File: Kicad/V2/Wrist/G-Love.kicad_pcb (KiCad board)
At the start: 2 copper layers, 36 x 36 mm, 154 parts, among them J5 XLR5_Ground, U1 ATMega328P, U10 6N137, U11 MAX485E, U12 TPS2113APWR, U13 AMS1117, U2 ICM-42688-P_I2C, U3 TXS0104E, U4 Hall Sensor A3144, U5 ATMEGA2561-16AU, U6 TUSB321, U7 74HC4052, U8 74HC4052, U9 B0505S-1W1, Y1 16MHz, Y2 16MHz

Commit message: j'aurai du commit avant, j'ai tunnel
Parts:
- removed C24, C25, C26, C33, C34, C35, C36, C37, C39, C40, C42, C43, C47, C49, C51: 100nF, MyGlove:Capacitor_0603
- removed C27, C28: 47pF, MyGlove:Capacitor_0603
- removed C29, C30, C38, C41, C48: 4.7uF, MyGlove:Capacitor_Electrolytic
- removed C31: 10nF, MyGlove:Capacitor_0603
- removed C32: 10n, MyGlove:Capacitor_0603
- removed C44, C45, C46: 1uF, MyGlove:Capacitor_0603
- removed C50: 10uF, MyGlove:Capacitor_0603
- removed D2, D5, D6: YELLOW, MyGlove:LED
- removed D3, D4: RED, MyGlove:LED
- removed FSR_1, FSR_2, FSR_3, FSR_4, FSR_5, FS_1, FS_2, FS_3, FS_4, FS_5, FS_6: ~, MyGlove:PinHeader_1x02_P2.54mm_Vertical
- removed J4: ~, MyGlove:PinHeader_1x06_P2.54mm_Vertical
- removed J5: XLR5_Ground, MyGlove:XLR5_Connector_Female_CONN-TH_NC5FAH
- removed J_1, J_2: Conn_USB_Receptacle, MyGlove:USB_C_Receptacle_GCT_USB4105-xx-A_16P_TopMnt_Horizontal
- removed J_3: ~, MyGlove:PinHeader_1x04_P2.54mm_Vertical
- removed R19, R28, R37, R39: 10kΩ, MyGlove:Resistor_0603
- removed R20, R21, R30, R31, R32, R33: 1k, MyGlove:Resistor_0603
- removed R22, R23: 1M, MyGlove:Resistor_0603
- removed R24, R25, R26, R27: 5.1k, MyGlove:Resistor_0603
- removed R29: 900K, MyGlove:Resistor_0805
- removed R34: 330R, MyGlove:Resistor_0603
- removed R35: 4.7k, MyGlove:Resistor_0603
- removed R36: 560R, MyGlove:Resistor_0603
- removed R38: 47k, MyGlove:Resistor_0603
- removed the REF** at (212.2, 90.5)
- removed the REF** at (187.8, 90.5)
- removed the REF** at (187.8, 109.5)
- removed the REF** at (212.2, 109.5)
- removed SW_1, SW_2: ~, MyGlove:SW_SPST_TL3305A
- removed TP1, TP10, TP11, TP12, TP13, TP14, TP15, TP16, TP17, TP18, TP2, TP3, TP4, TP5, TP6, TP7, TP8, TP9: ~, MyGlove:TestPoint_Pad_D1.0mm
- removed U10: 6N137, MyGlove:6N137
- removed U11: MAX485E, MyGlove:MAX485ED
- removed U12: TPS2113APWR, MyGlove:TPS2113
- removed U13: AMS1117, MyGlove:AMS1117
- removed U3: TXS0104E, MyGlove:TXS0104EPWR
- removed U4: Hall Sensor A3144, MyGlove:PinHeader_1x03_P2.54mm_Vertical
- removed U5: ATMEGA2561-16AU, MyGlove:ATMega2561
- removed U6: TUSB321, Package_DFN_QFN:Texas_X2QFN-12_1.6x1.6mm_P0.4mm
- removed U7, U8: 74HC4052, MyGlove:74HC4052
- removed U9: B0505S-1W1, MyGlove:B0505S
- removed U_1: CH340K, MyGlove:CH340K
- removed Y2: 16MHz, MyGlove:Crystal_16MHz
- added J01: ~, MyGlove:FPC 14, F.Cu at (133.5, 91.5)
- added J04: SM12B-SRSS-TB(LF)(SN), MyGlove:JST 12 Pin, F.Cu at (187.0, 100.0)
- added J2: ~, MyGlove:PinHeader_1x06_P2.54mm_Vertical, F.Cu at (193.6, 116.5)
- added J6: ~, MyGlove:JST 4 Pin, F.Cu at (200.1, 85.9)
- added REF**: Watch mount hole, G-Love:Watch mount hole, F.Cu at (200.0, 100.0)
- added U03: TXS0102DCUR, MyGlove:LVL SHIFTER TXS0102DCUR, F.Cu at (208.2, 93.2)
- C10: value 0.1nF -> 12pF
- C11, C12: value 47pF -> 100nF
- C13, C14, C15, C16, C17, C18, C19: value 47pF -> 10nF
- C2: value 100nF -> 10uF
- C20, C21: value 12pF -> 10nF
- C22: value 100nF -> 10nF
- C6, C7: value 12pF -> 100nF
- C8: value 10nF -> 100nF
- C9: value 2.2nF -> 12pF
- CD1: footprint MyGlove:CD4097B -> MyGlove:CD4097BPW
- D1: value YELLOW -> ~; footprint MyGlove:LED -> MyGlove:TVS_DIODE
- J3: footprint MyGlove:PinHeader_1x11_P2.54mm_Vertical -> MyGlove:FPC_CONNECTOR_24
- R1, R2: value 2.2kΩ -> 2.2K
- R3: value 1K -> 10kΩ
- R4: value 1K -> 330R
- R5: value 10kΩ -> 330R
- R8: value 10kΩ -> 10K
- U1: value ATMega328P -> XC6206P332MR-G; footprint MyGlove:ATMega328P-AU -> MyGlove:LDO Mini
- U2: value ICM-42688-P_I2C -> ATMega328P; footprint MyGlove:ICM-42688-P -> MyGlove:ATMega328P-AU
- moved C11 111.6 mm to (207.4, 89.1), turned to 90 degrees
- moved R8 108.1 mm to (205.9, 94.3), turned to 90 degrees
- moved C20 97.1 mm to (206.7, 107.0), turned to 180 degrees
- moved C21 97.0 mm to (206.7, 108.5), turned to 180 degrees
- moved C22 97.0 mm to (206.7, 110.0), turned to 180 degrees
- moved R17 89.7 mm to (209.8, 108.5), turned to 180 degrees
- moved J3 87.0 mm to (212.7, 100.0), turned to -90 degrees
- moved C23 87.0 mm to (196.5, 113.9)
- moved R16 83.6 mm to (209.8, 107.0), turned to 180 degrees
- moved C19 78.5 mm to (206.7, 105.5), turned to 180 degrees
- moved R12 71.3 mm to (209.8, 101.0), turned to 180 degrees
- moved C15 66.3 mm to (206.7, 99.5), turned to 180 degrees
- moved C4 66.0 mm to (203.0, 98.9), turned to 180 degrees
- moved R5 61.3 mm to (200.7, 91.9)
- moved R18 60.7 mm to (209.8, 110.0), turned to 180 degrees
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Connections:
- C1 pad 1: GND -> VCC
- C1 pad 2: Net-(U1-AREF) -> GND
- C10 pad 1: +3.3V -> GND
- C10 pad 2: GND -> Net-(U2-XTAL2/TOSC2/PCINT7/PB7)
- C11 pad 1: GND -> +3.3V
- C11 pad 2: /Hand_Captors/Flex_Sensor4/FlexADC -> GND
- C12 pad 1: GND -> VCC
- C12 pad 2: /Hand_Captors/Flex_Sensor3/FlexADC -> GND
- C13 pad 1: GND -> /Hand_Captors/hand_captors/FORCE_THUMB_IN
- C13 pad 2: /Hand_Captors/Flex_Sensor2/FlexADC -> GND
- C14 pad 1: GND -> /Hand_Captors/hand_captors/FLEX_THUMB_IN
- C14 pad 2: /Hand_Captors/Flex_Sensor0/FlexADC -> GND
- C15 pad 1: GND -> /Hand_Captors/hand_captors/FORCE_INDEX_IN
- C15 pad 2: /Hand_Captors/FSR_Index/TouchADC -> GND
- C16 pad 1: GND -> /Hand_Captors/hand_captors/FLEX_INDEX_IN
- C16 pad 2: /Hand_Captors/FSR_Little/TouchADC -> GND
- C17 pad 1: GND -> /Hand_Captors/hand_captors/FORCE_MIDDLE_IN
- C17 pad 2: /Hand_Captors/FSR_Ring/TouchADC -> GND
- C18 pad 1: GND -> /Hand_Captors/hand_captors/FLEX_MIDDLE_IN
- C18 pad 2: /Hand_Captors/FSR_Thumb/TouchADC -> GND
- C19 pad 1: GND -> /Hand_Captors/hand_captors/FORCE_RING_IN
- C19 pad 2: /Hand_Captors/Flex_Sensor5/FlexADC -> GND
- C2 pad 2: VCC -> +3.3V
- C20 pad 1: Net-(U5-XTAL2) -> /Hand_Captors/hand_captors/FLEX_RING_IN
- C21 pad 1: GND -> /Hand_Captors/hand_captors/FORCE_LITTLE_IN
- C21 pad 2: Net-(U5-XTAL1) -> GND
- C22 pad 1: GND -> /Hand_Captors/hand_captors/FLEX_LITTLE_IN
- C22 pad 2: Net-(C22-Pad2) -> GND
- C23 pad 1: /ATMega2561/MCU_2561_RESET -> VCC
- C23 pad 2: /ATMega2561/DTR -> GND
- C3 pad 2: VCC -> +3.3V
- C4 pad 2: Net-(C4-Pad2) -> Net-(U2-AREF)
- C5 pad 1: VCC -> GND
- C5 pad 2: GND -> VCC
- C6 pad 2: Net-(U1-XTAL1/TOSC1/PCINT6/PB6) -> VCC
- C7 pad 2: Net-(U1-XTAL2/TOSC2/PCINT7/PB7) -> /ATmega328p/MCU_328P_RESET
- C8 pad 1: GND -> VCC
- C8 pad 2: +3.3V -> GND
- C9 pad 1: +3.3V -> GND
- C9 pad 2: GND -> Net-(U2-XTAL1/TOSC1/PCINT6/PB6)
- CD1 pad 18: /Hand_Captors/Flex_Sensor5/FlexADC -> /Hand_Captors/hand_captors/HALL_IN
- CD1 pad 19: /Hand_Captors/Flex_Sensor4/FlexADC -> /Hand_Captors/hand_captors/FORCE_LITTLE_IN
- CD1 pad 20: /Hand_Captors/Flex_Sensor3/FlexADC -> /Hand_Captors/hand_captors/FORCE_RING_IN
- CD1 pad 21: /Hand_Captors/Flex_Sensor2/FlexADC -> /Hand_Captors/hand_captors/FORCE_MIDDLE_IN
- CD1 pad 22: /Hand_Captors/Flex_Sensor1/FlexADC -> /Hand_Captors/hand_captors/FORCE_INDEX_IN
- CD1 pad 23: /Hand_Captors/Flex_Sensor0/FlexADC -> /Hand_Captors/hand_captors/FORCE_THUMB_IN
- CD1 pad 4: /Hand_Captors/HallCaptor/HallGPIO_Clasp -> unconnected-(CD1-X_5-Pad4)
- CD1 pad 5: /Hand_Captors/FSR_Little/TouchADC -> /Hand_Captors/hand_captors/FLEX_LITTLE_IN
- CD1 pad 6: /Hand_Captors/FSR_Ring/TouchADC -> /Hand_Captors/hand_captors/FLEX_RING_IN
- CD1 pad 7: /Hand_Captors/FSR_Middle/TouchADC -> /Hand_Captors/hand_captors/FLEX_MIDDLE_IN
- CD1 pad 8: /Hand_Captors/FSR_Index/TouchADC -> /Hand_Captors/hand_captors/FLEX_INDEX_IN
- CD1 pad 9: /Hand_Captors/FSR_Thumb/TouchADC -> /Hand_Captors/hand_captors/FLEX_THUMB_IN
- D1 pad 1: Net-(D1-A) -> /ATmega328p/MISO_BOOT_328P
- D1 pad 2: /ATMega2561/2561_TXD1 -> /ATmega328p/SCK_BOOT_328P
- J3 pad 1: GND -> VCCL
- J3 pad 10: /ATMega2561/2561_MOSI -> Net-(U03-A2)
- J3 pad 11: VCC -> GND
- J3 pad 2: /ATMega2561/2561_TOUCH_INT -> VCCL
- J3 pad 3: /ATMega2561/2561_TOUCH_RESET -> GND
- J3 pad 4: /ATMega2561/2561_SDA -> GND
- J3 pad 5: /ATMega2561/2561_SCL -> /ATmega328p/MISO_BOOT_328P
- J3 pad 6: /ATMega2561/2561_SS -> /ATmega328p/SCK_BOOT_328P
- J3 pad 7: /ATMega2561/2561_SCREEN_DC -> GND
- J3 pad 8: /ATMega2561/2561_SCREEN_RESET -> +3.3V
- J3 pad 9: /ATMega2561/SCK_BOOT_2561 -> Net-(U03-A1)
- R1 pad 1: /ATMega2561/2561_SCL -> /ATmega328p/328P_I2C_IMU_SDA
- R10 pad 1: /Hand_Captors/Flex_Sensor2/FlexADC -> /Hand_Captors/hand_captors/FLEX_THUMB_IN
- R11 pad 1: /Hand_Captors/Flex_Sensor0/FlexADC -> /Hand_Captors/hand_captors/FORCE_INDEX_IN
- R12 pad 1: GND -> /Hand_Captors/hand_captors/FLEX_INDEX_IN
- R12 pad 2: /Hand_Captors/FSR_Index/TouchADC -> GND
- R13 pad 1: GND -> /Hand_Captors/hand_captors/FORCE_MIDDLE_IN
- R13 pad 2: /Hand_Captors/FSR_Little/TouchADC -> GND
- R14 pad 1: GND -> /Hand_Captors/hand_captors/FLEX_MIDDLE_IN
- R14 pad 2: /Hand_Captors/FSR_Ring/TouchADC -> GND
- R15 pad 1: GND -> /Hand_Captors/hand_captors/FORCE_RING_IN
- R15 pad 2: /Hand_Captors/FSR_Thumb/TouchADC -> GND
- R16 pad 1: /Hand_Captors/Flex_Sensor5/FlexADC -> /Hand_Captors/hand_captors/FLEX_RING_IN
- R17 pad 1: /ATMega2561/MCU_2561_RESET -> /Hand_Captors/hand_captors/FORCE_LITTLE_IN
- R17 pad 2: VCC -> GND
- R18 pad 1: /Hand_Captors/Flex_Sensor1/FlexADC -> /Hand_Captors/hand_captors/FLEX_LITTLE_IN
- R2 pad 1: /ATMega2561/2561_SDA -> /ATmega328p/328P_I2C_IMU_SCL
- R3 pad 1: Net-(D1-A) -> /ATmega328p/MCU_328P_RESET
- R4 pad 1: Net-(D2-A) -> Net-(U2-OC2A/MOSI/PCINT3/PB3)
- R4 pad 2: VCC -> /ATmega328p/MISO_BOOT_328P
- R5 pad 1: /ATmega328p/MCU_328P_RESET -> Net-(U2-SCK/PCINT5/PB5)
- R5 pad 2: VCC -> /ATmega328p/SCK_BOOT_328P
- R8 pad 1: /Hand_Captors/Flex_Sensor4/FlexADC -> /Hand_Captors/hand_captors/HALL_IN
- R8 pad 2: GND -> VCC
- R9 pad 1: /Hand_Captors/Flex_Sensor3/FlexADC -> /Hand_Captors/hand_captors/FORCE_THUMB_IN
- U1 pad 1: unconnected-(U1-OC2B/INT1/PCINT19/PD3-Pad1) -> GND
- U1 pad 2: unconnected-(U1-XCK/T0/PCINT20/PD4-Pad2) -> +3.3V
- U1 pad 3: GND -> VCC
- U2 pad 11: GND -> unconnected-(U2-AIN1/PCINT23/PD7-Pad11)
- U2 pad 12: +3.3V -> unconnected-(U2-ICP1/CLK0/PCINT0/PB0-Pad12)
- U2 pad 13: Net-(U2-AP_SCK) -> unconnected-(U2-OC1A/PCINT1/PB1-Pad13)
- U2 pad 14: Net-(U2-AP_SDA) -> unconnected-(U2-OC1B/~{SS}/PCINT2/PB2-Pad14)
- U2 pad 3: unconnected-(U2-RESV-Pad3) -> GND
- U2 pad 4: unconnected-(U2-INT1/INT-Pad4) -> VCC
- U2 pad 5: +3.3V -> GND
- U2 pad 6: GND -> VCC
- U2 pad 7: GND -> Net-(U2-XTAL1/TOSC1/PCINT6/PB6)
- U2 pad 8: +3.3V -> Net-(U2-XTAL2/TOSC2/PCINT7/PB7)
- Y1 pad 1: Net-(U1-XTAL1/TOSC1/PCINT6/PB6) -> Net-(U2-XTAL1/TOSC1/PCINT6/PB6)
- Y1 pad 3: Net-(U1-XTAL2/TOSC2/PCINT7/PB7) -> Net-(U2-XTAL2/TOSC2/PCINT7/PB7)
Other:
- board size 36 x 36 mm -> 39 x 39 mm
- board text added: "Ajouter Testpoints / 0Ohm pour reverse, 0603 en série"

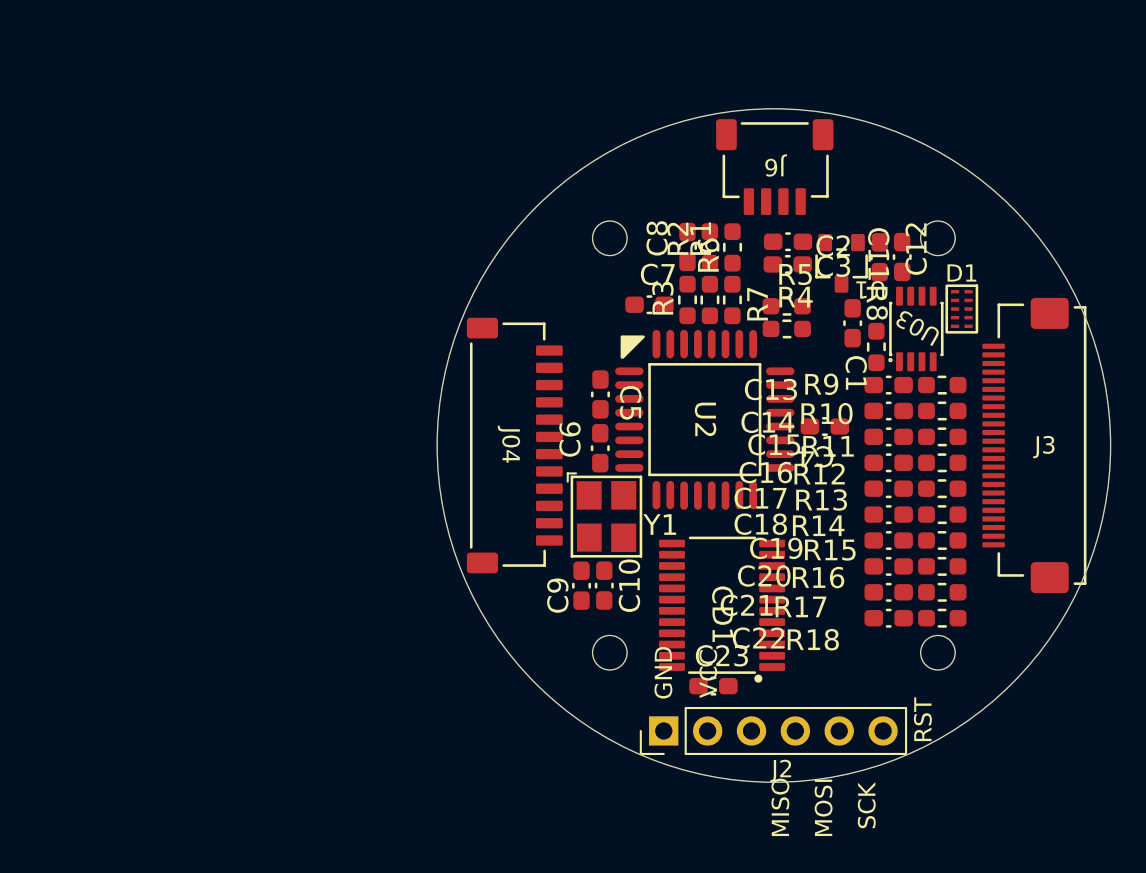
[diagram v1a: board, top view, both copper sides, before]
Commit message: Routing ADC
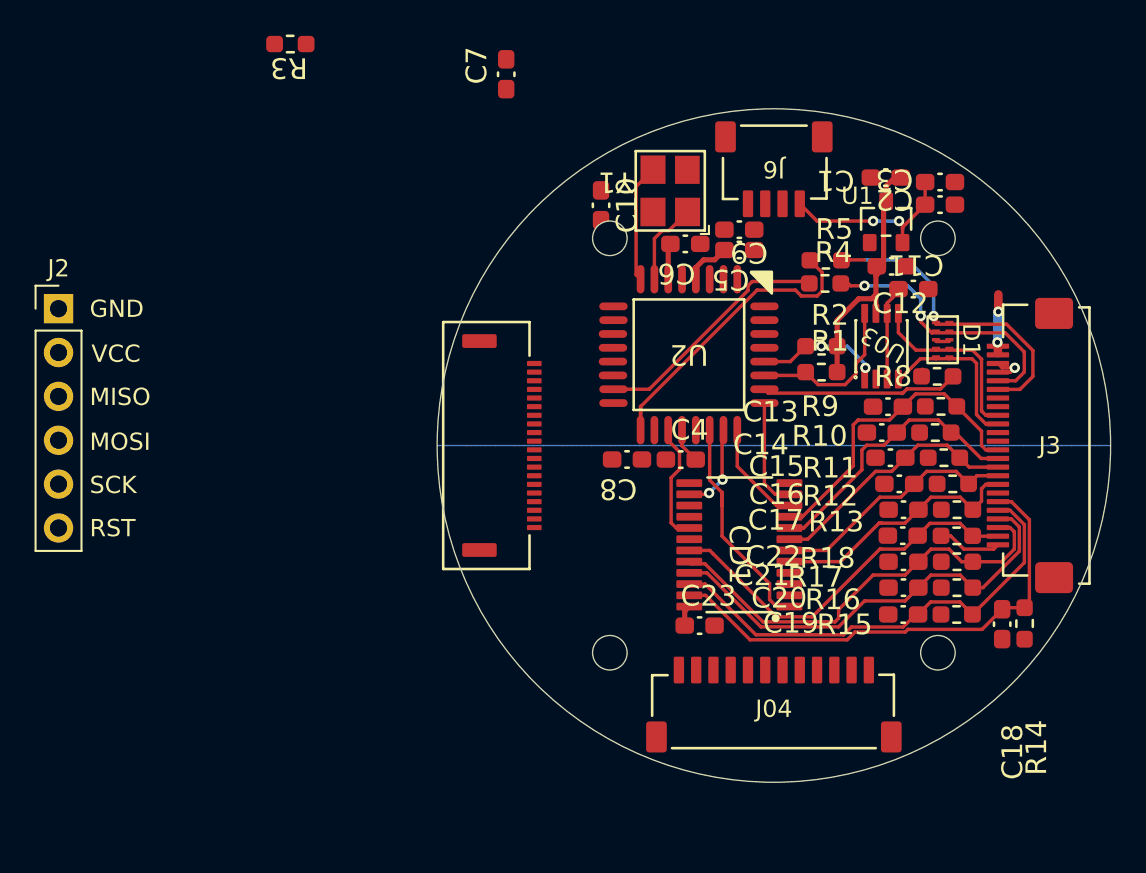
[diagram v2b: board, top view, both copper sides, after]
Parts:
- removed R6, R7: 2.2kΩ, MyGlove:Resistor_0603
- added J05: ~, MyGlove:FPC 20_2561_328P, F.Cu at (182.9, 100.0)
- moved J2 42.7 mm to (158.6, 92.1), turned to 0 degrees
- moved R3 27.4 mm to (172.0, 76.8), turned to 180 degrees
- moved C9 22.6 mm to (198.0, 87.5), turned to 180 degrees
- moved C10 22.0 mm to (190.0, 86.1)
- moved Y1 19.2 mm to (194.0, 85.2), turned to 90 degrees
- moved J04 18.4 mm to (200.0, 113.0), turned to 0 degrees
- moved C7 15.7 mm to (184.5, 78.5), turned to 90 degrees
- moved C6 12.8 mm to (194.9, 88.3), turned to 180 degrees
- moved C8 12.8 mm to (191.5, 100.8), turned to 180 degrees
- moved C5 11.6 mm to (198.0, 88.7), turned to 180 degrees
- moved C3 10.0 mm to (209.6, 84.7), turned to 180 degrees
- moved C18 9.13 mm to (213.2, 110.3), turned to -90 degrees
- moved C2 9.06 mm to (209.6, 86.1), turned to 180 degrees
- moved R1 8.87 mm to (202.8, 95.8), turned to 0 degrees
- moved C1 8.65 mm to (206.5, 84.5), turned to 180 degrees
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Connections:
- CD1 pad 13: /ATmega328p/328P_ADC_MUX_INH -> GND
- CD1 pad 18: /Hand_Captors/hand_captors/HALL_IN -> unconnected-(CD1-Y_5-Pad18)
- CD1 pad 19: /Hand_Captors/hand_captors/FORCE_LITTLE_IN -> /Hand_Captors/hand_captors/FLEX_LITTLE_IN
- CD1 pad 20: /Hand_Captors/hand_captors/FORCE_RING_IN -> /Hand_Captors/hand_captors/FORCE_LITTLE_IN
- CD1 pad 21: /Hand_Captors/hand_captors/FORCE_MIDDLE_IN -> /Hand_Captors/hand_captors/FLEX_RING_IN
- CD1 pad 22: /Hand_Captors/hand_captors/FORCE_INDEX_IN -> /Hand_Captors/hand_captors/FORCE_RING_IN
- CD1 pad 23: /Hand_Captors/hand_captors/FORCE_THUMB_IN -> /Hand_Captors/hand_captors/FLEX_MIDDLE_IN
- CD1 pad 5: /Hand_Captors/hand_captors/FLEX_LITTLE_IN -> /Hand_Captors/hand_captors/FORCE_MIDDLE_IN
- CD1 pad 6: /Hand_Captors/hand_captors/FLEX_RING_IN -> /Hand_Captors/hand_captors/FLEX_INDEX_IN
- CD1 pad 7: /Hand_Captors/hand_captors/FLEX_MIDDLE_IN -> /Hand_Captors/hand_captors/FORCE_INDEX_IN
- CD1 pad 8: /Hand_Captors/hand_captors/FLEX_INDEX_IN -> /Hand_Captors/hand_captors/FLEX_THUMB_IN
- CD1 pad 9: /Hand_Captors/hand_captors/FLEX_THUMB_IN -> /Hand_Captors/hand_captors/FORCE_THUMB_IN
- D1 pad 1: /ATmega328p/MISO_BOOT_328P -> /ATmega328p/SCK_BOOT_328P
- D1 pad 2: /ATmega328p/SCK_BOOT_328P -> /ATmega328p/MISO_BOOT_328P
- J3 pad 12: /Hand_Captors/hand_captors/HALL_IN -> /ATmega328p/HALL
- R8 pad 1: /Hand_Captors/hand_captors/HALL_IN -> /ATmega328p/HALL
- U2 pad 23: /ATmega328p/328P_ADC_MUX_SELECT_B -> /ATmega328p/328P_ADC_MUX_SELECT_C
- U2 pad 24: /ATmega328p/328P_ADC_MUX_SELECT_C -> /ATmega328p/328P_ADC_MUX_SELECT_A
- U2 pad 25: /ATmega328p/328P_ADC_MUX_SELECT_A -> /ATmega328p/328P_ADC_MUX_SELECT_B
- U2 pad 26: /ATmega328p/328P_ADC_MUX_INH -> /ATmega328p/HALL
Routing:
- net /Hand_Captors/hand_captors/FLEX_MIDDLE_IN: track 0.00 -> 28.7 mm
- net /Hand_Captors/hand_captors/FORCE_RING_IN: track 0.00 -> 27.0 mm
- net /Hand_Captors/hand_captors/FLEX_RING_IN: track 0.00 -> 25.7 mm
- net /Hand_Captors/hand_captors/FORCE_LITTLE_IN: track 0.00 -> 25.0 mm
- net /Hand_Captors/hand_captors/FLEX_LITTLE_IN: track 0.00 -> 22.1 mm
- net VCC: track 0.00 -> 21.2 mm
- net Net-(U2-SCK/PCINT5/PB5): track 0.00 -> 18.4 mm
- net /Hand_Captors/hand_captors/FORCE_THUMB_IN: track 0.00 -> 18.2 mm
- net /ATmega328p/SCK_BOOT_328P: track 0.00 -> 17.9 mm, vias 0 -> 1
- net +3.3V: track 0.00 -> 16.3 mm, vias 0 -> 2
- net /Hand_Captors/hand_captors/FLEX_THUMB_IN: track 0.00 -> 16.3 mm
- net /ATmega328p/MISO_BOOT_328P: track 0.00 -> 15.5 mm, vias 0 -> 2
- net /Hand_Captors/hand_captors/FORCE_MIDDLE_IN: track 0.00 -> 15.1 mm
- net /Hand_Captors/hand_captors/FORCE_INDEX_IN: track 0.00 -> 14.9 mm
- net /Hand_Captors/hand_captors/FLEX_INDEX_IN: track 0.00 -> 14.5 mm
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- added copper zone on B.Cu, net GND

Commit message: Routing Quasi fini
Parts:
- added TP5: ~, MyGlove:TestPoint_Pad_D1.0mm, F.Cu at (188.1, 96.2)
- added TP6: ~, MyGlove:TestPoint_Pad_D1.0mm, F.Cu at (188.0, 93.0)
- added TP7: ~, MyGlove:TestPoint_Pad_D1.0mm, F.Cu at (188.1, 94.6)
- moved R3 21.2 mm to (187.9, 90.8)
- moved C7 11.5 mm to (187.9, 89.5), turned to 0 degrees
- moved C10 1.31 mm to (191.0, 85.2), turned to -90 degrees
- moved C8 0.69 mm to (190.9, 101.1)
- moved U2 0.69 mm to (194.4, 95.0)
- moved C4 0.69 mm to (194.0, 101.1)
- moved C6 0.61 mm to (194.9, 88.9)
- moved R1 0.50 mm to (202.8, 96.2)
- moved R2 0.50 mm to (202.8, 94.8)
- moved U1 0.30 mm to (206.5, 86.8)
- moved C1 0.30 mm to (206.5, 84.2)
- moved C5 0.26 mm to (198.0, 88.9)
- moved C9 0.17 mm to (198.0, 87.7)
- moved C12 0.12 mm to (206.8, 89.5)
- moved C11 0.06 mm to (208.1, 91.0)
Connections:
- J04 pad : GND -> (no net)
- U2 pad 12: unconnected-(U2-ICP1/CLK0/PCINT0/PB0-Pad12) -> Net-(U2-ICP1/CLK0/PCINT0/PB0)
- U2 pad 9: unconnected-(U2-OC0B/T1/PCINT21/PD5-Pad9) -> Net-(U2-OC0B/T1/PCINT21/PD5)
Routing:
- net VCC: track 21.2 -> 89.8 mm, vias 0 -> 10
- net +3.3V: track 16.3 -> 62.6 mm, vias 2 -> 6
- net VCCL: track 3.43 -> 43.4 mm, vias 2 -> 6
- net /FingerTip Modules/FingerTip_I2C_SCL: track 0.00 -> 22.7 mm, vias 0 -> 2
- net /FingerTip Modules/FingerTip_I2C_SDA: track 0.00 -> 22.1 mm, vias 0 -> 2
- net /ATmega328p/328P_TX: track 0.00 -> 16.3 mm, vias 0 -> 4
- net /ATmega328p/328P_RX: track 0.00 -> 16.2 mm, vias 0 -> 4
- net /ATmega328p/MCU_328P_RESET: track 0.00 -> 15.3 mm, vias 0 -> 2
- net GND: track 6.65 -> 15.6 mm, vias 1 -> 2
- net Net-(U2-XTAL1/TOSC1/PCINT6/PB6): track 4.91 -> 11.1 mm
- net Net-(U2-XTAL2/TOSC2/PCINT7/PB7): track 6.86 -> 9.70 mm
- net /ATmega328p/MOSI_BOOT_328P: track 0.00 -> 2.72 mm
- net Net-(U2-OC0B/T1/PCINT21/PD5): track 0.00 -> 2.39 mm
- net Net-(U2-ICP1/CLK0/PCINT0/PB0): track 0.00 -> 2.01 mm
- net /ATmega328p/SCK_BOOT_328P: track 17.9 -> 19.8 mm, vias 1 -> 0
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
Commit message: DRC en cours
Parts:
- removed J2: ~, MyGlove:PinHeader_1x06_P2.54mm_Vertical
- moved R9 0.37 mm to (209.3, 97.8)
- moved C13 0.36 mm to (206.2, 97.8)
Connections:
- J04 pad : (no net) -> GND
- J04 pad 1: /Touchscreen/Screen_SPI_SCK -> /Touchscreen/Touch_RESET
- J04 pad 2: /Touchscreen/Screen_SPI_MOSI -> /Touchscreen/Touch_I2C_INT
- J04 pad 6: /FingerTip Modules/FingerTip_I2C_SCL -> /Touchscreen/Screen_SPI_MOSI
- J04 pad 7: /FingerTip Modules/FingerTip_I2C_SDA -> /Touchscreen/Screen_SPI_SCK
- J04 pad 8: /Touchscreen/Touch_RESET -> /FingerTip Modules/FingerTip_I2C_SDA
- J04 pad 9: /Touchscreen/Touch_I2C_INT -> /FingerTip Modules/FingerTip_I2C_SCL
- J05 pad : (no net) -> GND
- J3 pad : (no net) -> GND
- J6 pad : (no net) -> GND
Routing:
- net GND: track 15.6 -> 93.4 mm, vias 2 -> 96
- net /FingerTip Modules/FingerTip_I2C_SCL: track 22.7 -> 56.4 mm
- net /FingerTip Modules/FingerTip_I2C_SDA: track 22.1 -> 53.6 mm
- net /Touchscreen/Screen_SPI_SCK: track 0.00 -> 29.0 mm
- net /Touchscreen/Screen_SPI_MOSI: track 0.00 -> 26.8 mm
- net /Touchscreen/Screen_SPI_SS: track 0.00 -> 23.1 mm
- net /Touchscreen/Screen_D/C: track 0.00 -> 16.5 mm
- net /Touchscreen/Screen_RESET: track 0.00 -> 15.2 mm
- net /Touchscreen/Touch_I2C_INT: track 0.00 -> 13.8 mm
- net /Touchscreen/Touch_RESET: track 0.00 -> 12.5 mm
- net /ATmega328p/HALL: track 12.4 -> 18.2 mm
- net /Hand_Captors/hand_captors/FORCE_INDEX_IN: track 14.9 -> 15.7 mm
- net /Hand_Captors/hand_captors/FLEX_THUMB_IN: track 16.3 -> 17.0 mm
- net /Hand_Captors/hand_captors/FLEX_LITTLE_IN: track 22.1 -> 22.9 mm

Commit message: DRC bon, reste serigraphie
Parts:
- added TP8: ~, MyGlove:TestPoint_Pad_D1.0mm, F.Cu at (201.0, 88.0)
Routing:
- net GND: track 93.4 -> 72.2 mm, vias 96 -> 86
- net Net-(U2-OC2A/MOSI/PCINT3/PB3): track 14.6 -> 17.3 mm
- net /ATmega328p/328P_TX: track 16.3 -> 17.3 mm
- net VCC: track 89.6 -> 90.5 mm, vias 10 -> 9
- added copper zone on F.Cu, net GND
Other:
- board size 39 x 39 mm -> 40 x 40 mm
- board text removed: "Ajouter Testpoints / 0Ohm pour reverse, 0603 en série"

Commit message: DRC bon
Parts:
- added TP10: ~, MyGlove:TestPoint_Pad_D1.25mm, F.Cu at (190.3, 90.2)
- added TP9: ~, MyGlove:TestPoint_Pad_D1.25mm, F.Cu at (200.8, 92.0)
- TP5, TP6, TP7, TP8: footprint MyGlove:TestPoint_Pad_D1.0mm -> MyGlove:TestPoint_Pad_D1.25mm
- moved TP6 0.14 mm to (188.2, 93.1)
- moved TP5 0.10 mm to (188.1, 96.3)
- moved TP7 0.09 mm to (188.1, 94.7)
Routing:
- net Net-(U2-SCK/PCINT5/PB5): track 18.1 -> 19.9 mm
- net VCC: track 90.5 -> 91.4 mm
- net GND: vias 86 -> 87
